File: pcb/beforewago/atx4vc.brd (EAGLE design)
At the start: 86 x 70 mm, 69 parts, among them IC2 REG1117, IC3 STM32F042F4, IC4 MY_7905DT, J1 ATX24RH, SW1 324_SW, SW2 324_SW, SW3 324_SW, SW4 324_SW, SW5 324_SW, SW7 324_SW, U1 USBC_16P, U2 USBC_16P

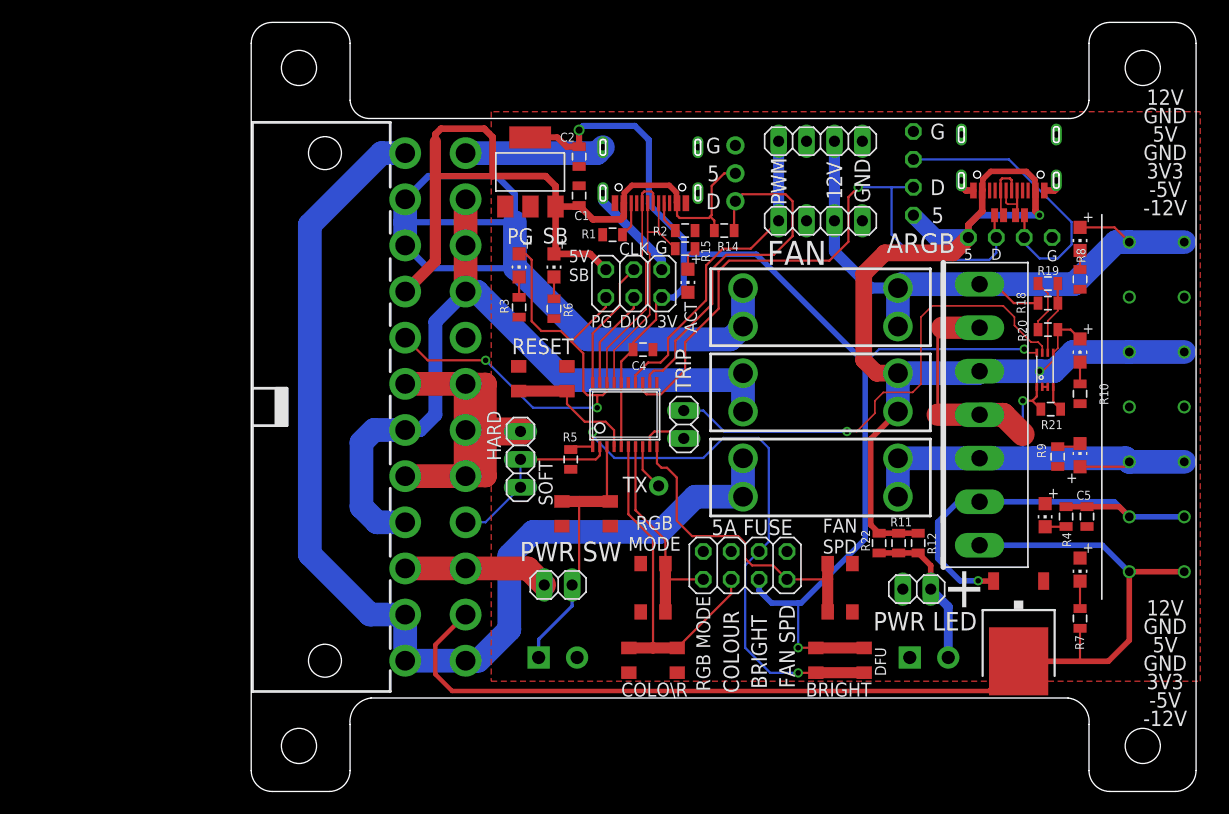
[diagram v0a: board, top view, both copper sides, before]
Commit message: switched to WAGO connectors
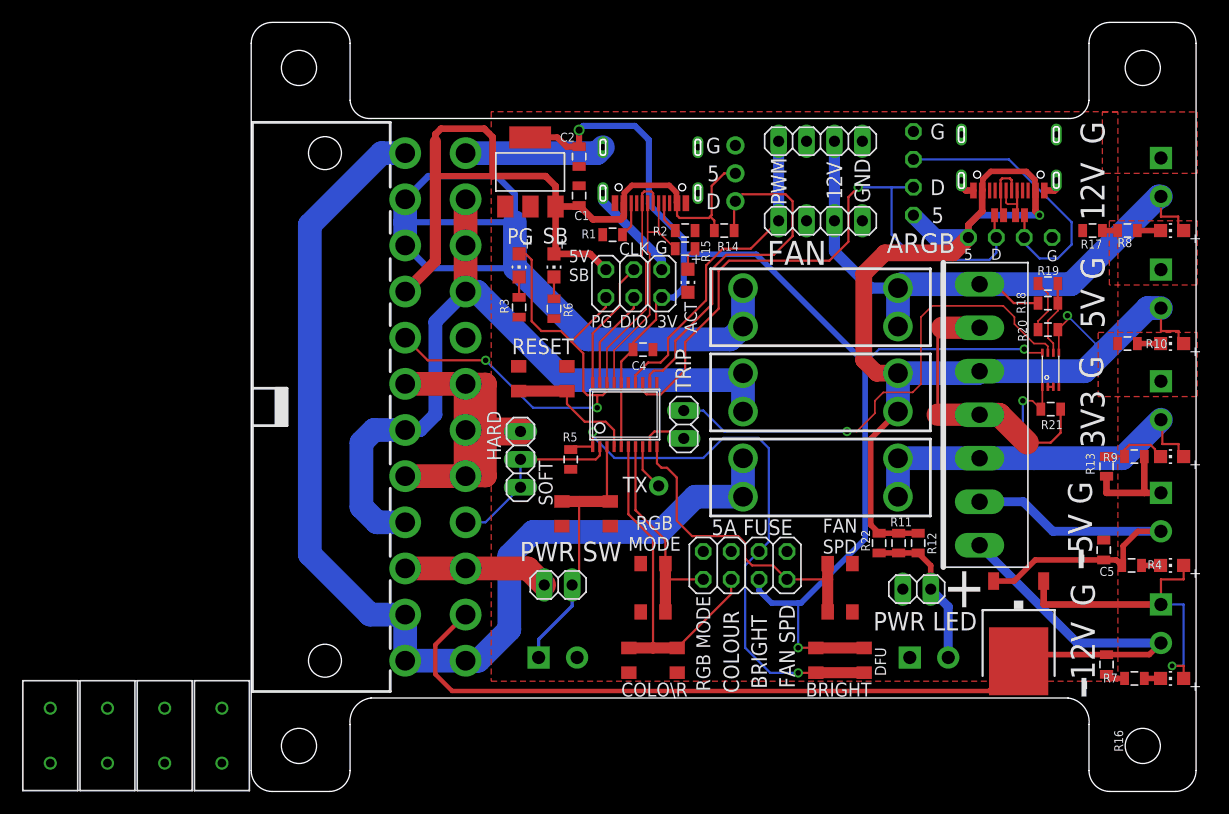
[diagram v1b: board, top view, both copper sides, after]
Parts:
- added J2, J3, J4, J6: (no value), atx_power_control:SCREWTERMINAL-3.5MM-2
- added J7: (no value), atx_power_control:SCREWTERMINAL-3.5MM-2-NS
- added R13, R17: 5K1, atx_power_control:0805
- added R16: 5K1, SparkFun-Passives:0805
- added U$11, U$12, U$13: WAGO257, atx4vc:WAGL257
- U$9: value WAGO257-7 -> WAGO257; device atx4vc:WAGO257-7 -> atx4vc:WAGL257
- moved U$9 90.2 mm to (-2.67, 5.08), turned to 0 degrees
- moved LED4 13.0 mm to (83.8, 10.3), turned to 90 degrees
- moved LED1 12.4 mm to (83.8, 20.6), turned to 90 degrees
- moved LED5 8.42 mm to (83.8, 51.1), turned to 90 degrees
- moved LED7 8.41 mm to (83.8, 40.8), turned to 90 degrees
- moved LED6 8.38 mm to (83.8, 30.5), turned to 90 degrees
- moved R4 7.44 mm to (80.1, 20.6), turned to 0 degrees
- moved R7 7.37 mm to (80.4, 10.3), turned to 0 degrees
- moved R9 6.98 mm to (80.4, 30.5), turned to 180 degrees
- moved R10 6.29 mm to (79.8, 40.8), turned to 0 degrees
- moved R8 6.20 mm to (79.8, 51.1), turned to 0 degrees
- moved C5 3.41 mm to (77.6, 22.0), turned to 270 degrees
- moved U$6 0.51 mm to (72.0, 36.8)
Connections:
- removed net -12V: IC4.3, J1.14, R7.1, U$4.P$1, U$9.P$1, U$9.P$2
- removed net -5V: C5.2, IC4.2, R4.1, U$4.P$2, U$9.P$3, U$9.P$4
- new net N$11: C5.2, IC4.2, J4.2, R4.1, U$4.P$2
- new net N$2: IC4.3, J1.14, J3.2, R16.1, U$4.P$1
- new net N$28: R16.2, R7.1
- new net N$32: R17.2, R8.1
- net F12V: now also J6.2; no longer U$9.P$13, U$9.P$14
- net F3V3: now also J2.2; no longer U$9.P$5, U$9.P$6
- net F5V: now also J7.2; no longer U$9.P$10, U$9.P$9
- net GND: now also J2.1, J3.1, J4.1, J6.1, J7.1, R13.1, R17.1; no longer R8.1, U$9.P$11, U$9.P$12, U$9.P$7, U$9.P$8
- net N$18: now also R13.2
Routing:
- net -12V: track 101.1 -> 0.00 mm
- net N$2: track 0.00 -> 95.2 mm
- net GND: track 101.8 -> 144.8 mm, vias 0 -> 1
- net -5V: track 39.2 -> 0.00 mm, vias 1 -> 0
- net N$11: track 0.00 -> 36.1 mm
- net F5V: track 104.1 -> 110.4 mm
- net N$18: track 2.15 -> 6.27 mm
- net N$28: track 0.00 -> 1.79 mm
- net N$32: track 0.00 -> 1.38 mm
- net N$8: track 2.50 -> 1.48 mm
- net F3V3: track 43.4 -> 44.0 mm
- net +3V3: track 122.1 -> 122.7 mm
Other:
- board text added: "-12V"
- board text added: "-5V"
- board text added: "3V3"
- board text added: "5V"
- board text removed: "12V GND 5V GND 3V3 -5V -12V"
